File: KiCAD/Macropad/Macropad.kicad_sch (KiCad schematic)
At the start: 17 parts, among them SW1 SW_Push_45deg, SW2 SW_Push_45deg, SW3 SW_Push_45deg, SW4 SW_Push_45deg, SW5 SW_Push_45deg, SW6 SW_Push_45deg, SW7 EC1110120201, U1 XIAO-RP2040-DIP, U2 SSD1306

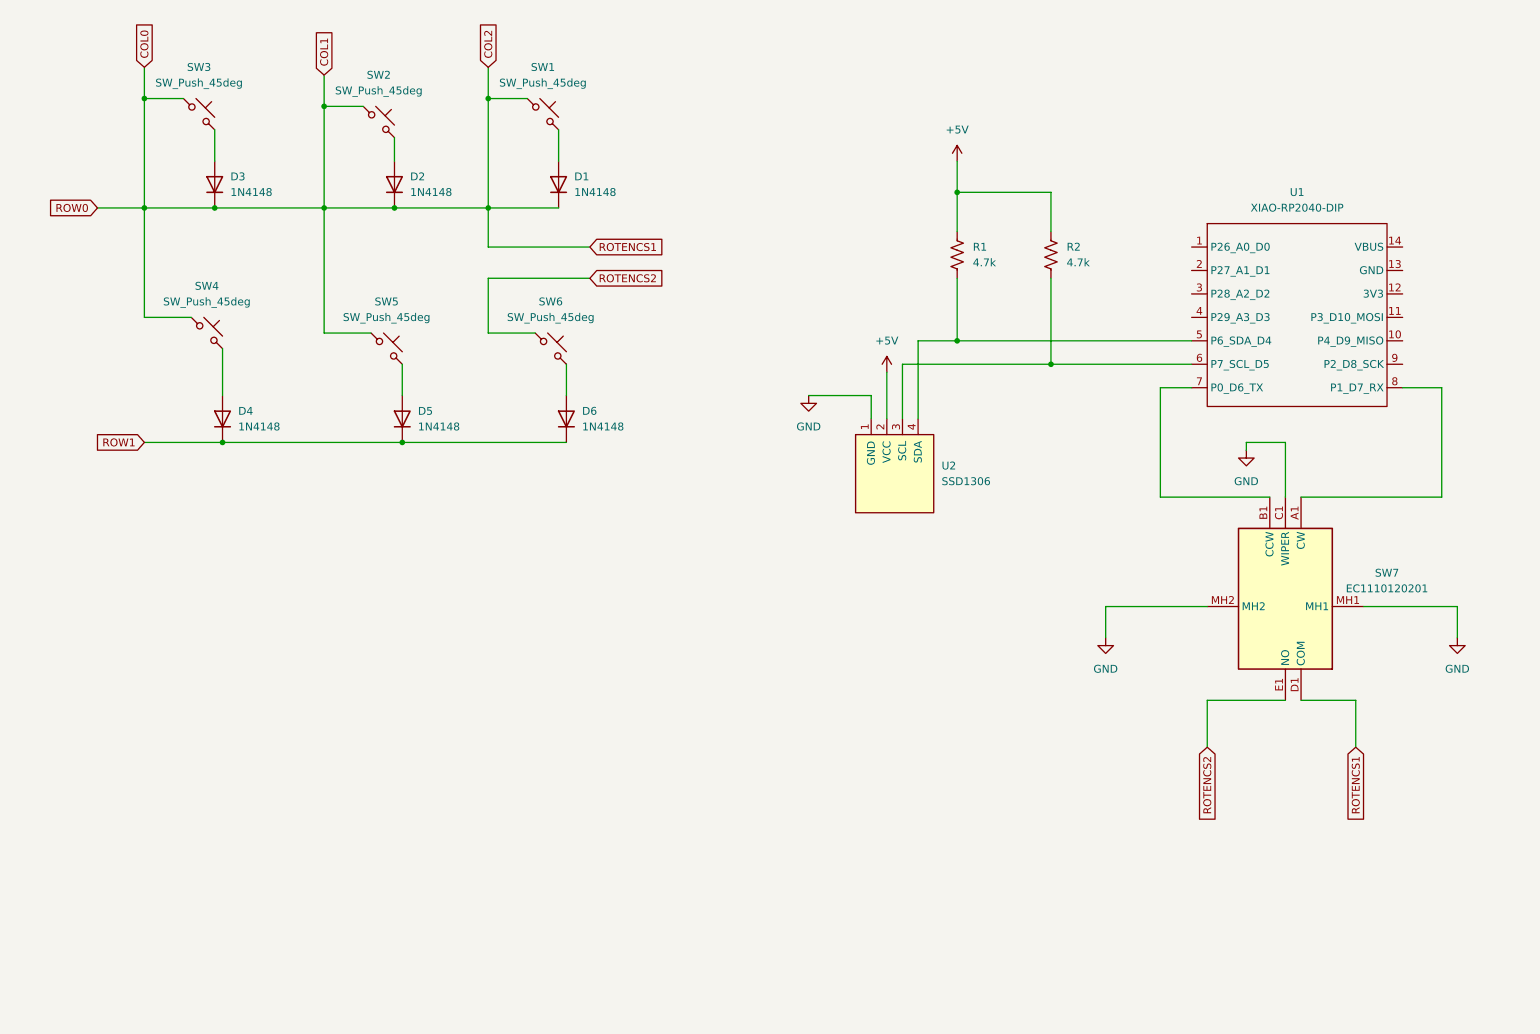
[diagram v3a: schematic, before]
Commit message: Added diodes and ports, finished schematic :D.
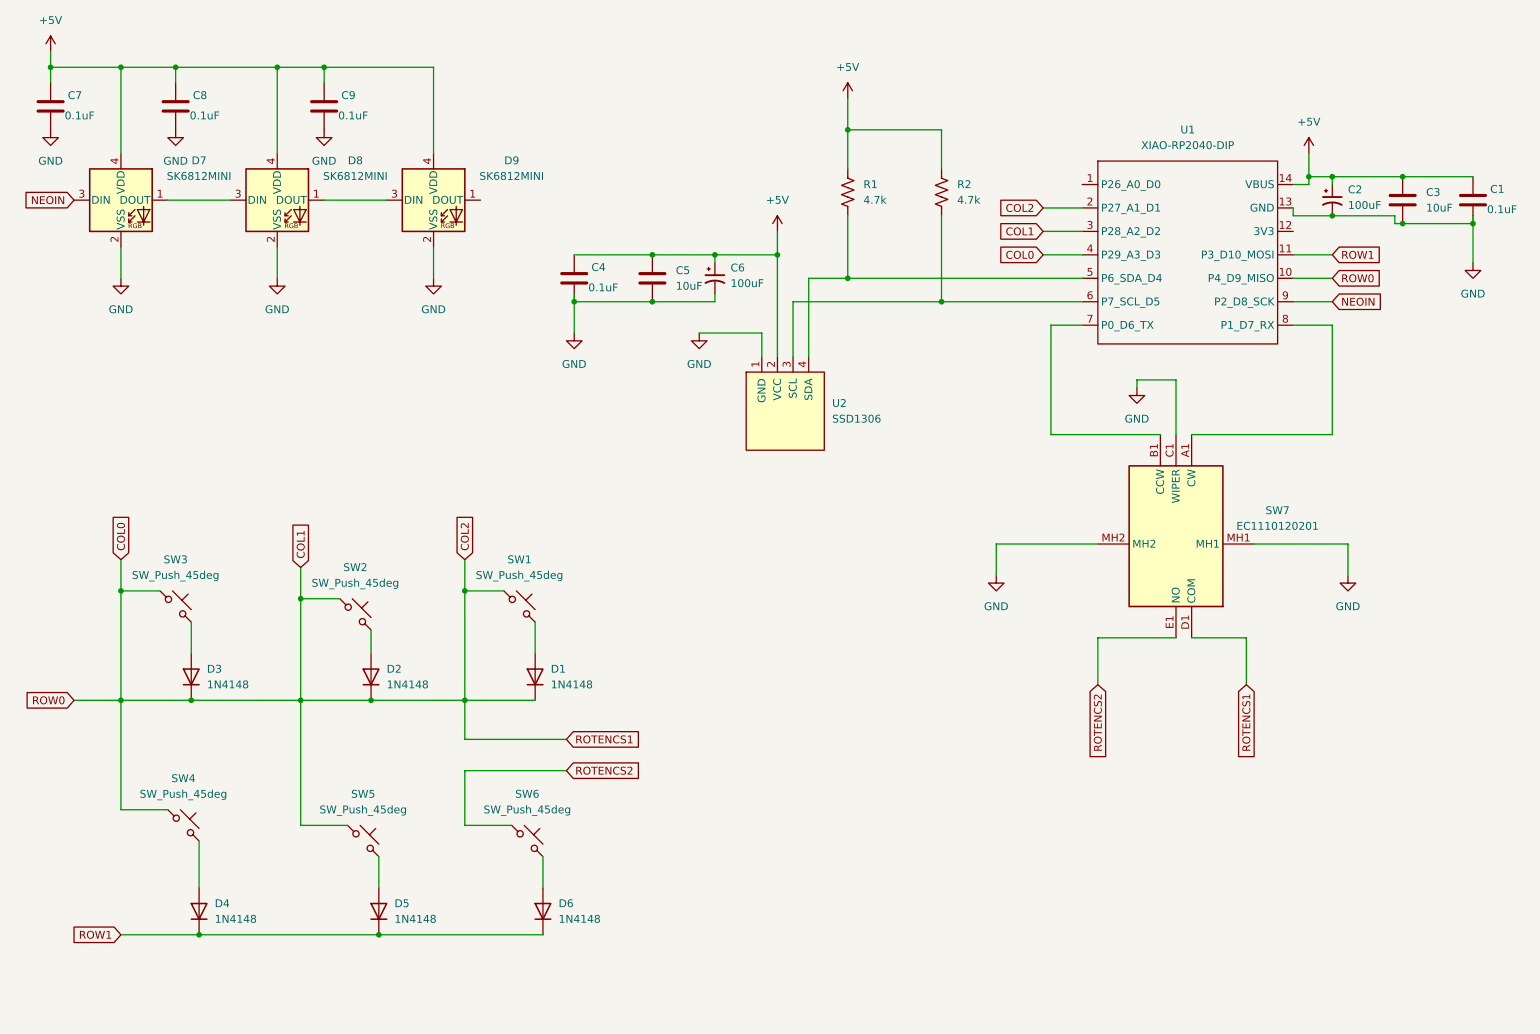
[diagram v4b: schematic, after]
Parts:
- added C1, C4, C7, C8, C9: 0.1uF, Capacitor_THT:C_Disc_D3.8mm_W2.6mm_P2.50mm, symbol Device:C
- added C2, C6: 100uF, Capacitor_THT:CP_Radial_Tantal_D6.0mm_P2.50mm, symbol Device:C_Polarized_Small_US
- added C3, C5: 10uF, Capacitor_THT:C_Disc_D4.7mm_W2.5mm_P5.00mm, symbol Device:C
- added D7, D8, D9: SK6812MINI, LED_SMD:LED_SK6812MINI_PLCC4_3.5x3.5mm_P1.75mm, symbol LED:SK6812MINI
- D1, D2, D3, D4, D5, D6: Part_Number (none) -> 1N4148FS-ND; Vendor (none) -> Digi-Key
- SW1, SW2, SW3, SW4, SW5, SW6: footprint (none) -> Button_Switch_Keyboard:SW_Cherry_MX_1.00u_PCB; Part_Number (none) -> 1644-MX2A-E1NW-ND; Vendor (none) -> Digi-Key
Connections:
- net +5V: now also U1.14 (VBUS), C1.1, C2.1, C3.1, C4.1, C5.1, C6.1, C7.1, C8.1, C9.1, D7.4 (VDD), D8.4 (VDD), D9.4 (VDD)
- net COL0: now also U1.10 (P4_D9_MISO), U1.2 (P27_A1_D1), U1.3 (P28_A2_D2), U1.4 (P29_A3_D3)
- net GND: now also U1.13 (GND), C1.2, C2.2, C3.2, C4.2, C5.2, C6.2, C7.2, C8.2, C9.2, D7.2 (VSS), D8.2 (VSS), D9.2 (VSS)
- net ROW1: now also U1.11 (P3_D10_MOSI)
- net NEOIN: now reaches U1.9 (P2_D8_SCK)
- net NEOIN: now also D7.3 (DIN)
- new net: D8.1 (DOUT), D9.3 (DIN)
- new net: D7.1 (DOUT), D8.3 (DIN)
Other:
- moved on the sheet: D3, R1, R2, SW3, SW7, U1, U2

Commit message: Added footprints for rotary encoder and rp2040.
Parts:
- SW7: footprint EC1110120201 -> EC1110120201_Rotary_Encoder:EC1110120201
- U1: footprint Seeed_Studio_XIAO_Series:XIAO-RP2040-DIP -> XIAO_Series_Footprints:XIAO-RP2350-DIP; Part_Number https://www.amazon.com/Microcontroller-Dual-Core-MicroPytho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 -> 1597-102010428-ND; Vendor Amazon -> Digi-Key
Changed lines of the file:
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@@
 			)
 		)
-		(property "Footprint" "EC1110120201"
+		(property "Footprint" "EC1110120201_Rotary_Encoder:EC1110120201"
 			(at 201.93 19.38 0)
 			(effects
@@
 			)
 		)
-		(property "Footprint" "Seeed_Studio_XIAO_Series:XIAO-RP2040-DIP"
+		(property "Footprint" "XIAO_Series_Footprints:XIAO-RP2350-DIP"
 			(at 214.884 76.708 0)
 			(effects
@@
 			)
 		)
-		(property "Datasheet" ""
+		(property "Datasheet" "https://files.seeedstudio.com/wiki/XIAO-RP2040/res/rp2040_datasheet.pdf"
 			(at 210.82 39.37 0)
 			(effects
@@
 			)
 		)
-		(property "Vendor" "Amazon"
+		(property "Vendor" "Digi-Key"
 			(at 210.82 39.37 0)
 			(effects
@@
 			)
 		)
-		(property "Part_Number" "https://www.amazon.com/Microcontroller-Dual-Core-MicroPython-CircuitPython-Interfaces/dp/B0DRNTQ338?th=1"
+		(property "Part_Number" "1597-102010428-ND"
 			(at 210.82 39.37 0)
 			(effects

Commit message: Initial candidate for layout
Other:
- moved on the sheet: D1, D2, D3, D4, D5, D6, SW1, SW2, SW3, SW4, SW5, SW6

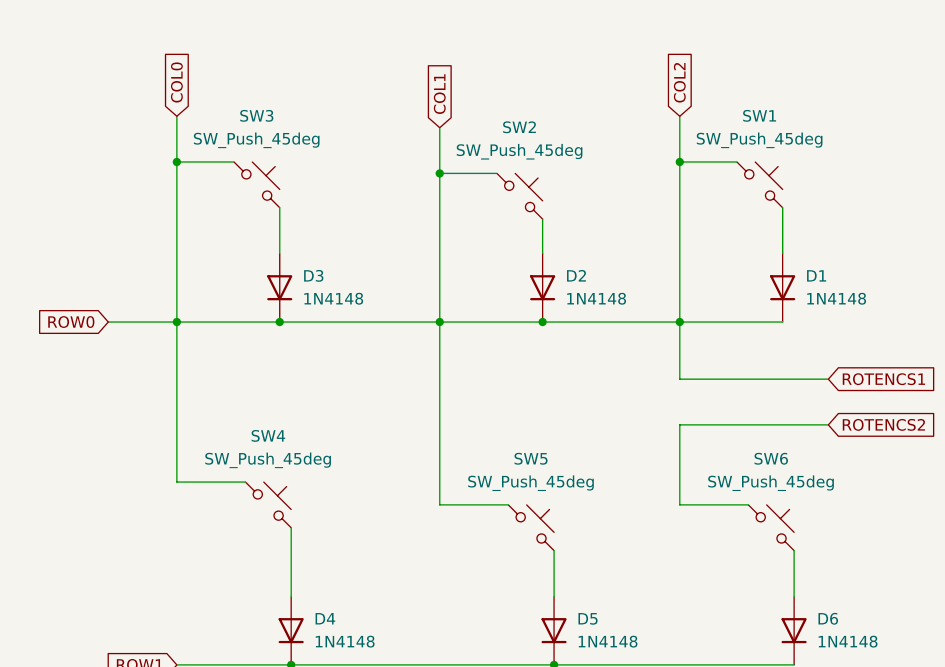
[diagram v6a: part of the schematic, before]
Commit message: Fixed some shorts in the matrix.
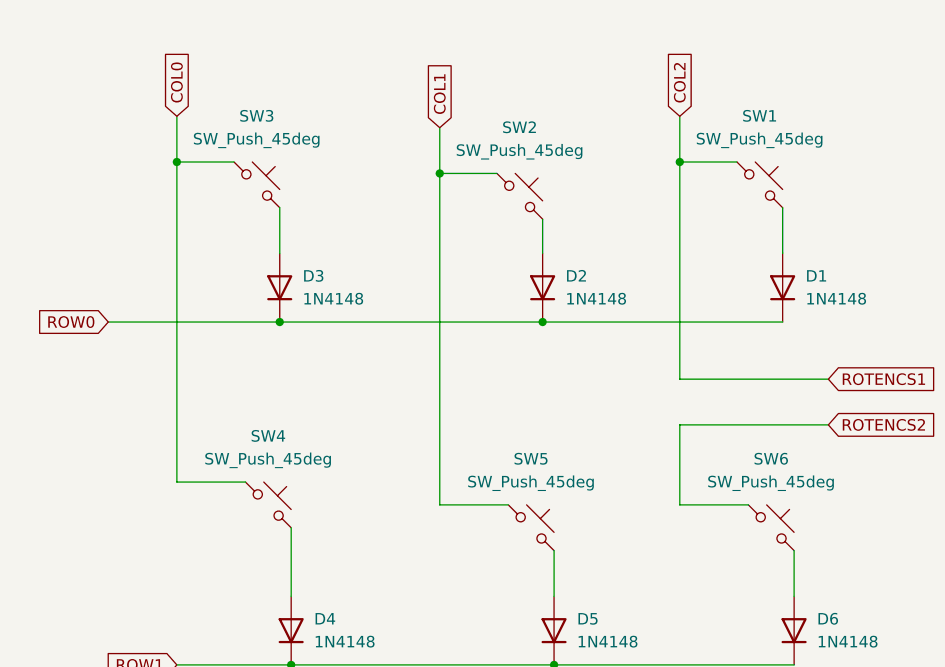
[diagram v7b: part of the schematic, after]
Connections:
- net COL0: no longer D1.1 (K), D2.1 (K), D3.1 (K), SW1.1, SW2.1, SW5.1, SW7.D1 (COM), U1.10 (P4_D9_MISO), U1.2 (P27_A1_D1), U1.3 (P28_A2_D2)
- new net COL1: SW2.1, SW5.1, U1.3 (P28_A2_D2)
- new net COL2: SW1.1, SW7.D1 (COM), U1.2 (P27_A1_D1)
- new net ROW0: D1.1 (K), D2.1 (K), D3.1 (K), U1.10 (P4_D9_MISO)
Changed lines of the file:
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@@
 	)
 	(junction
+		(at 39.37 127)
+		(diameter 0)
+		(color 0 0 0 0)
+	)
+	(junction
 		(at 236.22 46.99)
 		(diameter 0)
@@
 	)
 	(junction
-		(at 236.22 53.34)
+		(at 68.58 128.27)
 		(diameter 0)
 		(color 0 0 0 0)
 	)
 	(junction
-		(at 50.8 144.78)
+		(at 236.22 53.34)
 		(diameter 0)
 		(color 0 0 0 0)
 	)
 	(junction
-		(at 247.65 54.61)
+		(at 50.8 144.78)
 		(diameter 0)
 		(color 0 0 0 0)
 	)
 	(junction
-		(at 39.37 127)
+		(at 247.65 54.61)
 		(diameter 0)
 		(color 0 0 0 0)
@@
 	)
 	(junction
-		(at 95.25 127)
-		(diameter 0)
-		(color 0 0 0 0)
-	)
-	(junction
 		(at 48.26 29.21)
 		(diameter 0)
@@
 	)
 	(junction
-		(at 68.58 144.78)
-		(diameter 0)
-		(color 0 0 0 0)
-	)
-	(junction
 		(at 113.03 67.31)
 		(diameter 0)
@@
 	)
 	(junction
-		(at 39.37 144.78)
-		(diameter 0)
-		(color 0 0 0 0)
-	)
-	(junction
 		(at 259.08 54.61)
 		(diameter 0)
@@
 	)
 	(junction
-		(at 68.58 128.27)
+		(at 95.25 127)
 		(diameter 0)
 		(color 0 0 0 0)
@@
 	)
 	(junction
-		(at 95.25 144.78)
-		(diameter 0)
-		(color 0 0 0 0)
-	)
-	(junction
 		(at 146.05 59.69)
 		(diameter 0)
@@
 	(wire
 		(pts
-			(xy 39.37 144.78) (xy 39.37 162.56)
-		)
-		(stroke
-			(width 0)
-			(type default)
-		)
-	)
-	(wire
-		(pts
 			(xy 259.08 54.61) (xy 259.08 60.96)
 		)
@@
 	(wire
 		(pts
-			(xy 31.75 144.78) (xy 39.37 144.78)
-		)
-		(stroke
-			(width 0)
-			(type default)
-		)
-	)
-	(wire
-		(pts
 			(xy 223.52 106.68) (xy 238.76 106.68)
 		)
@@
 	(wire
 		(pts
-			(xy 95.25 127) (xy 95.25 144.78)
-		)
-		(stroke
-			(width 0)
-			(type default)
-		)
-	)
-	(wire
-		(pts
 			(xy 181.61 106.68) (xy 181.61 111.76)
 		)
@@
 	(wire
 		(pts
-			(xy 190.5 71.12) (xy 195.58 71.12)
+			(xy 95.25 127) (xy 95.25 151.13)
 		)
 		(stroke
@@
 	(wire
 		(pts
-			(xy 95.25 121.92) (xy 95.25 127)
+			(xy 190.5 71.12) (xy 195.58 71.12)
 		)
 		(stroke
@@
 	(wire
 		(pts
-			(xy 146.05 55.88) (xy 146.05 59.69)
+			(xy 95.25 121.92) (xy 95.25 127)
 		)
 		(stroke
@@
 	(wire
 		(pts
-			(xy 64.77 58.42) (xy 64.77 63.5)
+			(xy 146.05 55.88) (xy 146.05 59.69)
 		)
 		(stroke
@@
 	(wire
 		(pts
-			(xy 232.41 46.99) (xy 232.41 48.26)
+			(xy 64.77 58.42) (xy 64.77 63.5)
 		)
 		(stroke
@@
 	(wire
 		(pts
-			(xy 232.41 46.99) (xy 236.22 46.99)
+			(xy 232.41 46.99) (xy 232.41 48.26)
 		)
 		(stroke
@@
 	(wire
 		(pts
-			(xy 190.5 88.9) (xy 190.5 71.12)
+			(xy 232.41 46.99) (xy 236.22 46.99)
 		)
 		(stroke
@@
 	(wire
 		(pts
-			(xy 95.25 144.78) (xy 95.25 151.13)
+			(xy 190.5 88.9) (xy 190.5 71.12)
 		)
 		(stroke
@@
 	(wire
 		(pts
-			(xy 39.37 144.78) (xy 50.8 144.78)
+			(xy 31.75 144.78) (xy 50.8 144.78)
 		)
 		(stroke
@@
 	(wire
 		(pts
-			(xy 68.58 144.78) (xy 68.58 165.1)
-		)
-		(stroke
-			(width 0)
-			(type default)
-		)
-	)
-	(wire
-		(pts
 			(xy 157.48 45.72) (xy 157.48 39.37)
 		)
@@
 	(wire
 		(pts
-			(xy 68.58 128.27) (xy 68.58 144.78)
-		)
-		(stroke
-			(width 0)
-			(type default)
-		)
-	)
-	(wire
-		(pts
 			(xy 27.94 29.21) (xy 39.37 29.21)
 		)
@@
 	(wire
 		(pts
-			(xy 68.58 144.78) (xy 50.8 144.78)
-		)
-		(stroke
-			(width 0)
-			(type default)
-		)
-	)
-	(wire
-		(pts
 			(xy 208.28 88.9) (xy 190.5 88.9)
 		)
@@
 	(wire
 		(pts
-			(xy 68.58 144.78) (xy 80.01 144.78)
+			(xy 50.8 144.78) (xy 80.01 144.78)
 		)
 		(stroke
@@
 	(wire
 		(pts
-			(xy 95.25 151.13) (xy 111.76 151.13)
-		)
-		(stroke
-			(width 0)
-			(type default)
-		)
-	)
-	(wire
-		(pts
 			(xy 135.89 67.31) (xy 135.89 66.04)
 		)
@@
 	(wire
 		(pts
-			(xy 80.01 144.78) (xy 95.25 144.78)
+			(xy 80.01 144.78) (xy 106.68 144.78)
 		)
 		(stroke
@@
 	(wire
 		(pts
-			(xy 246.38 54.61) (xy 247.65 54.61)
+			(xy 95.25 151.13) (xy 111.76 151.13)
 		)
 		(stroke
@@
 	(wire
 		(pts
-			(xy 125.73 59.69) (xy 135.89 59.69)
+			(xy 246.38 54.61) (xy 247.65 54.61)
 		)
 		(stroke
@@
 	(wire
 		(pts
-			(xy 157.48 53.34) (xy 157.48 63.5)
+			(xy 125.73 59.69) (xy 135.89 59.69)
 		)
 		(stroke
@@
 	(wire
 		(pts
-			(xy 95.25 156.21) (xy 95.25 165.1)
+			(xy 157.48 53.34) (xy 157.48 63.5)
 		)
 		(stroke
@@
 	(wire
 		(pts
-			(xy 238.76 106.68) (xy 238.76 111.76)
+			(xy 95.25 156.21) (xy 95.25 165.1)
 		)
 		(stroke
@@
 	(wire
 		(pts
-			(xy 111.76 156.21) (xy 95.25 156.21)
+			(xy 238.76 106.68) (xy 238.76 111.76)
 		)
 		(stroke
@@
 	(wire
 		(pts
-			(xy 50.8 137.16) (xy 50.8 132.08)
+			(xy 111.76 156.21) (xy 95.25 156.21)
 		)
 		(stroke
@@
 	(wire
 		(pts
-			(xy 46.99 162.56) (xy 39.37 162.56)
+			(xy 50.8 137.16) (xy 50.8 132.08)
 		)
 		(stroke
@@
 	(wire
 		(pts
-			(xy 39.37 127) (xy 39.37 144.78)
+			(xy 46.99 162.56) (xy 39.37 162.56)
 		)
 		(stroke
@@
 	(wire
 		(pts
-			(xy 95.25 144.78) (xy 106.68 144.78)
+			(xy 68.58 123.19) (xy 68.58 128.27)
 		)
 		(stroke
@@
 	(wire
 		(pts
-			(xy 68.58 123.19) (xy 68.58 128.27)
+			(xy 68.58 128.27) (xy 68.58 165.1)
 		)
 		(stroke
@@
 	(wire
 		(pts
+			(xy 39.37 127) (xy 39.37 162.56)
+		)
+		(stroke
+			(width 0)
+			(type default)
+		)
+	)
+	(wire
+		(pts
 			(xy 229.87 53.34) (xy 229.87 52.07)
 		)
@@
 		)
 		(instances
-			(project ""
+			(project "Macropad"
 				(path "/50acfae0-7f10-4bf7-8da6-440d0ff2b716"
 					(reference "SW3")
@@
 		)
 		(instances
-			(project ""
+			(project "Macropad"
 				(path "/50acfae0-7f10-4bf7-8da6-440d0ff2b716"
 					(reference "D3")
@@
 		)
 		(instances
-			(project ""
+			(project "Macropad"
 				(path "/50acfae0-7f10-4bf7-8da6-440d0ff2b716"
 					(reference "#PWR04")
@@
 		)
 		(instances
-			(project ""
+			(project "Macropad"
 				(path "/50acfae0-7f10-4bf7-8da6-440d0ff2b716"
 					(reference "SW7")
@@
 		)
 		(instances
-			(project ""
+			(project "Macropad"
 				(path "/50acfae0-7f10-4bf7-8da6-440d0ff2b716"
 					(reference "#PWR05")
@@
 		)
 		(instances
-			(project ""
+			(project "Macropad"
 				(path "/50acfae0-7f10-4bf7-8da6-440d0ff2b716"
 					(reference "#PWR01")
@@
 		)
 		(instances
-			(project ""
+			(project "Macropad"
 				(path "/50acfae0-7f10-4bf7-8da6-440d0ff2b716"
 					(reference "D7")
@@
 		)
 		(instances
-			(project ""
+			(project "Macropad"
 				(path "/50acfae0-7f10-4bf7-8da6-440d0ff2b716"
 					(reference "U1")
